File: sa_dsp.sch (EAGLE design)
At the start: 409 parts, among them CN1 uSD, CN2 MINI B USB, CN3 2X5 HEADER, CN4 MINI B USB, CN5 USB A, CN6 MINI B USB, Q1 2N7002, Q2 2N7002, Q3 2N7002, Q4 2N7002, SW1 1825910-7, U1 PGA2311, U10 LME49720, U11 PGA2311, U12 LME49720, U13 LME49720, U14 PCM1754, U15 LME49720, U16 PGA2311, U17 LME49720, U18 LME49720, U19 PCM1754, U2 LM317, U20 LME49720, U21 7 SEG, U22 74HC164A, U23 PCM2707, U24 PCM2707, U25 7 SEG, U26 74HC164A, U27 LM337, U28 LM317, U29 7 SEG, U3 OSD3358-512M-BSM, U30 74HC164A, U31 100MHz, U32 USBLC6-2SC6, U33 FT230X, U34 USBLC6-2SC6, U35 USBLC6-2SC6, U36 USBLC6-2SC6, U37 2 PORT HUB, U38 TPS70925, U39 LM22670, U4 LME49720, U40 MPM3820, U41 MPM3820, U5 LME49720, U6 10CL016YF484C6G, U7 7 SEG, U8 74HC164A, U9 PCM1754

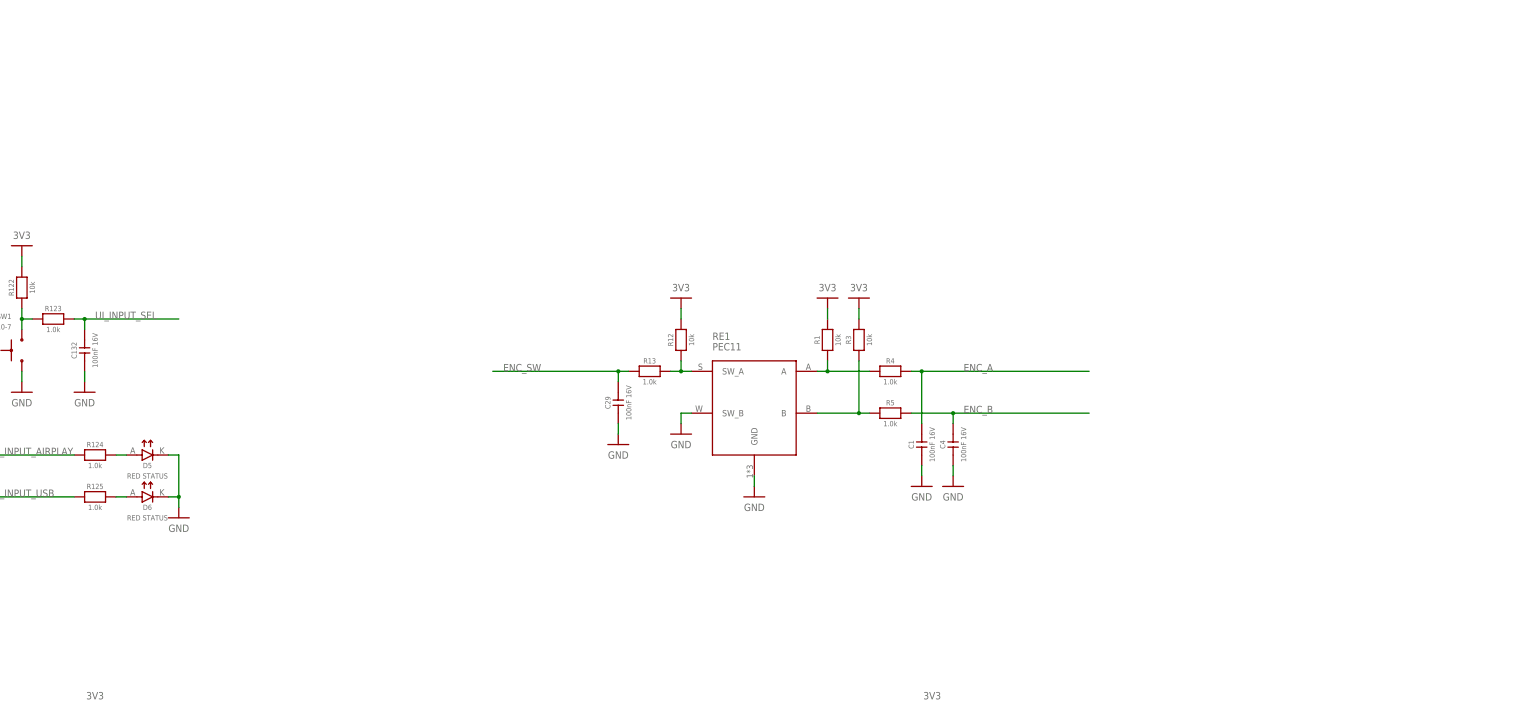
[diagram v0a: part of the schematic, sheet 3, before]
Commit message: Schmit triggers done, FPGA conf done
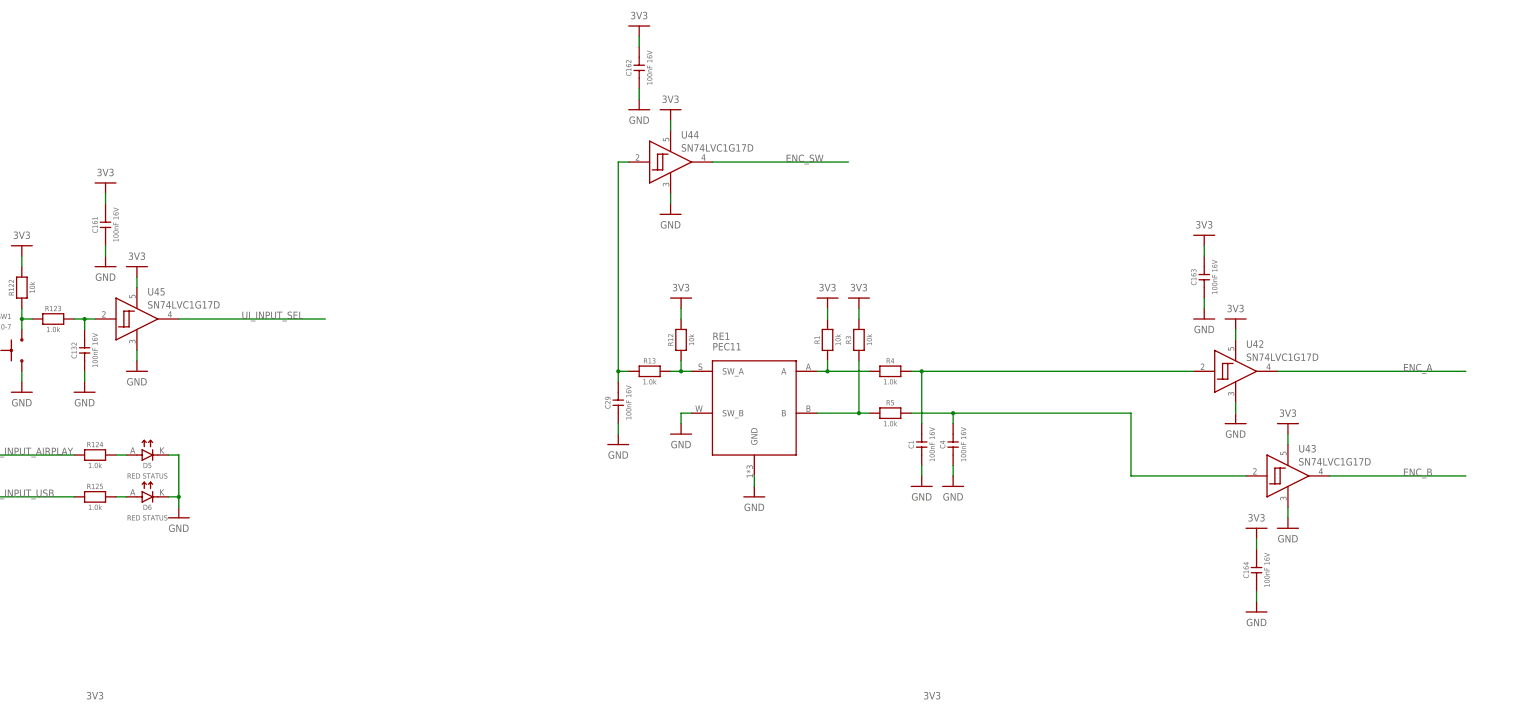
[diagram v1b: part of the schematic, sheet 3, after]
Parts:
- added C161, C162, C163, C164: 100nF 16V, CAPACITORS:CL10B104KO8WPNC
- added U42, U43, U44, U45: SN74LVC1G17D, ICs:SN74LVC1G17DBVR
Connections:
- new net N$238: C4.2, R5.2, U43.A
- new net N$239: C1.2, R4.2, U42.A
- new net N$240: C29.2, R13.1, U44.A
- new net N$241: C132.2, R123.2, U45.A
- net 3V3: now also C161.2, C162.2, C163.2, C164.2, U42.VCC, U43.VCC, U44.VCC, U45.VCC
- net DISP_SPI_!CE: now also U6.B8_IO29
- net DISP_SPI_MOSI: now also U6.B8_IO24
- net DISP_SPI_SCLK: now also U6.B8_IO15
- net ENC_A: now also U42.Q, U6.B8_IO33; no longer C1.2, R4.2
- net ENC_B: now also U43.Q, U6.B8_IO13; no longer C4.2, R5.2
- net ENC_SW: now also U44.Q, U6.B8_IO30; no longer C29.2, R13.1
- net GND: now also C161.1, C162.1, C163.1, C164.1, U42.GND, U43.GND, U44.GND, U45.GND
- net PGA1_SDI: now also U6.B6_IO14; no longer U6.B6_IO16
- net UI_INPUT_AIRPLAY: now also U6.B8_IO25
- net UI_INPUT_SEL: now also U45.Q; no longer C132.2, R123.2
- net UI_INPUT_USB: now also U6.B8_IO16

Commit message: Passes DRC
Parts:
- removed R87: 10k, r_0603:ERJ3EKF1002V
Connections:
- removed net CONF_NCONFIG: R87.1
- net 3V3: no longer R87.2
- net AM_PWR_BTN: now also U6.B2_IO14
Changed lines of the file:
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@@
 <part name="R85" library="r_0603" deviceset="ERJ3EKF1002V" device="" value="10k"/>
 <part name="R86" library="r_0603" deviceset="ERJ3EKF1002V" device="" value="10k"/>
-<part name="R87" library="r_0603" deviceset="ERJ3EKF1002V" device="" value="10k"/>
 <part name="U$163" library="NETS" deviceset="3V3" device=""/>
 <part name="U$164" library="NETS" deviceset="3V3" device=""/>
@@
 <part name="U$166" library="NETS" deviceset="3V3" device=""/>
 <part name="U$167" library="NETS" deviceset="3V3" device=""/>
-<part name="U$168" library="NETS" deviceset="3V3" device=""/>
 <part name="GND78" library="NETS" deviceset="GND" device=""/>
 <part name="GND79" library="NETS" deviceset="GND" device=""/>
@@
 <attribute name="VALUE" x="66.04" y="490.22" size="1.27" layer="96" rot="R90" align="center"/>
 </instance>
-<instance part="R87" gate="G$1" x="71.12" y="490.22" smashed="yes" rot="R90">
-<attribute name="NAME" x="68.58" y="490.22" size="1.27" layer="95" rot="R90" align="center"/>
-<attribute name="VALUE" x="73.66" y="490.22" size="1.27" layer="96" rot="R90" align="center"/>
-</instance>
 <instance part="U$163" gate="G$1" x="33.02" y="472.44" smashed="yes">
 <attribute name="VALUE" x="33.02" y="474.98" size="1.778" layer="96" rot="R180" align="center"/>
@@
 <instance part="U$167" gate="G$1" x="63.5" y="500.38" smashed="yes">
 <attribute name="VALUE" x="63.5" y="502.92" size="1.778" layer="96" rot="R180" align="center"/>
-</instance>
-<instance part="U$168" gate="G$1" x="71.12" y="500.38" smashed="yes">
-<attribute name="VALUE" x="71.12" y="502.92" size="1.778" layer="96" rot="R180" align="center"/>
 </instance>
 <instance part="GND78" gate="G$1" x="43.18" y="426.72" smashed="yes">
@@
 </segment>
 </net>
-<net name="CONF_NCONFIG" class="0">
-<segment>
-<pinref part="R87" gate="G$1" pin="1"/>
-<wire x1="71.12" y1="485.14" x2="71.12" y2="482.6" width="0.1524" layer="91"/>
-<wire x1="71.12" y1="482.6" x2="101.6" y2="482.6" width="0.1524" layer="91"/>
-<label x="73.66" y="482.6" size="1.778" layer="95"/>
-</segment>
-</net>
 <net name="CONF_NSTATUS" class="0">
 <segment>
@@
 <pinref part="U$167" gate="G$1" pin="3V3"/>
 <wire x1="63.5" y1="497.84" x2="63.5" y2="495.3" width="0.1524" layer="91"/>
-</segment>
-<segment>
-<pinref part="R87" gate="G$1" pin="2"/>
-<pinref part="U$168" gate="G$1" pin="3V3"/>
-<wire x1="71.12" y1="497.84" x2="71.12" y2="495.3" width="0.1524" layer="91"/>
 </segment>
 <segment>
@@
 </segment>
 </net>
+<net name="AM_PWR_BTN" class="0">
+<segment>
+<pinref part="U6" gate="G$1" pin="B2_IO14"/>
+<wire x1="312.42" y1="360.68" x2="350.52" y2="360.68" width="0.1524" layer="91"/>
+<label x="314.96" y="360.68" size="1.778" layer="95"/>
+</segment>
+</net>

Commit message: Analogue output connections added
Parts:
- added TP17, TP18, TP19, TP20, TP21, TP22, TP23, TP24, TP25, TP26, TP27, TP28, TP29, TP30, TP31, TP32, TP33, TP34: 2MM_TEST_POINT, MISC:2MM_TEST_POINT
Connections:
- net AGND: now also TP18.P$1, TP21.P$1, TP24.P$1, TP27.P$1, TP30.P$1, TP33.P$1
- net N$100: now also TP19.P$1
- net N$12: now also TP29.P$1
- net N$17: now also TP32.P$1
- net N$28: now also TP34.P$1
- net N$46: now also TP31.P$1
- net N$58: now also TP23.P$1
- net N$60: now also TP26.P$1
- net N$63: now also TP28.P$1
- net N$73: now also TP25.P$1
- net N$85: now also TP17.P$1
- net N$87: now also TP20.P$1
- net N$90: now also TP22.P$1
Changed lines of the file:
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@@
 <part name="GND181" library="NETS" deviceset="GND" device=""/>
 <part name="U$223" library="NETS" deviceset="3V3" device=""/>
+<part name="TP17" library="MISC" deviceset="2MM_TEST_POINT" device=""/>
+<part name="TP18" library="MISC" deviceset="2MM_TEST_POINT" device=""/>
+<part name="TP19" library="MISC" deviceset="2MM_TEST_POINT" device=""/>
+<part name="TP20" library="MISC" deviceset="2MM_TEST_POINT" device=""/>
+<part name="TP21" library="MISC" deviceset="2MM_TEST_POINT" device=""/>
+<part name="TP22" library="MISC" deviceset="2MM_TEST_POINT" device=""/>
+<part name="TP23" library="MISC" deviceset="2MM_TEST_POINT" device=""/>
+<part name="TP24" library="MISC" deviceset="2MM_TEST_POINT" device=""/>
+<part name="TP25" library="MISC" deviceset="2MM_TEST_POINT" device=""/>
+<part name="TP26" library="MISC" deviceset="2MM_TEST_POINT" device=""/>
+<part name="TP27" library="MISC" deviceset="2MM_TEST_POINT" device=""/>
+<part name="TP28" library="MISC" deviceset="2MM_TEST_POINT" device=""/>
+<part name="TP29" library="MISC" deviceset="2MM_TEST_POINT" device=""/>
+<part name="TP30" library="MISC" deviceset="2MM_TEST_POINT" device=""/>
+<part name="TP31" library="MISC" deviceset="2MM_TEST_POINT" device=""/>
+<part name="TP32" library="MISC" deviceset="2MM_TEST_POINT" device=""/>
+<part name="TP33" library="MISC" deviceset="2MM_TEST_POINT" device=""/>
+<part name="TP34" library="MISC" deviceset="2MM_TEST_POINT" device=""/>
+<part name="U$168" library="NETS" deviceset="AGND" device=""/>
 </parts>
 <sheets>
@@
 <attribute name="VALUE" x="43.18" y="657.86" size="1.27" layer="96" rot="MR0" align="center-left"/>
 </instance>
+<instance part="TP17" gate="G$1" x="457.2" y="662.94" smashed="yes" rot="R270">
+<attribute name="NAME" x="459.74" y="662.94" size="1.27" layer="97" rot="R270" align="center"/>
+</instance>
+<instance part="TP18" gate="G$1" x="474.98" y="647.7" smashed="yes" rot="R270">
+<attribute name="NAME" x="477.52" y="647.7" size="1.27" layer="97" rot="R270" align="center"/>
+</instance>
+<instance part="TP19" gate="G$1" x="457.2" y="632.46" smashed="yes" rot="R270">
+<attribute name="NAME" x="459.74" y="632.46" size="1.27" layer="97" rot="R270" align="center"/>
+</instance>
+<instance part="TP20" gate="G$1" x="457.2" y="591.82" smashed="yes" rot="R270">
+<attribute name="NAME" x="459.74" y="591.82" size="1.27" layer="97" rot="R270" align="center"/>
+</instance>
+<instance part="TP21" gate="G$1" x="474.98" y="579.12" smashed="yes" rot="R270">
+<attribute name="NAME" x="477.52" y="579.12" size="1.27" layer="97" rot="R270" align="center"/>
+</instance>
+<instance part="TP22" gate="G$1" x="457.2" y="561.34" smashed="yes" rot="R270">
+<attribute name="NAME" x="459.74" y="561.34" size="1.27" layer="97" rot="R270" align="center"/>
+</instance>
+<instance part="TP23" gate="G$1" x="457.2" y="408.94" smashed="yes" rot="R270">
+<attribute name="NAME" x="459.74" y="408.94" size="1.27" layer="97" rot="R270" align="center"/>
+</instance>
+<instance part="TP24" gate="G$1" x="474.98" y="396.24" smashed="yes" rot="R270">
+<attribute name="NAME" x="477.52" y="396.24" size="1.27" layer="97" rot="R270" align="center"/>
+</instance>
+<instance part="TP25" gate="G$1" x="457.2" y="378.46" smashed="yes" rot="R270">
+<attribute name="NAME" x="459.74" y="378.46" size="1.27" layer="97" rot="R270" align="center"/>
+</instance>
+<instance part="TP26" gate="G$1" x="457.2" y="337.82" smashed="yes" rot="R270">
+<attribute name="NAME" x="459.74" y="337.82" size="1.27" layer="97" rot="R270" align="center"/>
+</instance>
+<instance part="TP27" gate="G$1" x="474.98" y="327.66" smashed="yes" rot="R270">
+<attribute name="NAME" x="477.52" y="327.66" size="1.27" layer="97" rot="R270" align="center"/>
+</instance>
+<instance part="TP28" gate="G$1" x="457.2" y="307.34" smashed="yes" rot="R270">
+<attribute name="NAME" x="459.74" y="307.34" size="1.27" layer="97" rot="R270" align="center"/>
+</instance>
+<instance part="TP29" gate="G$1" x="457.2" y="154.94" smashed="yes" rot="R270">
+<attribute name="NAME" x="459.74" y="154.94" size="1.27" layer="97" rot="R270" align="center"/>
+</instance>
+<instance part="TP30" gate="G$1" x="474.98" y="142.24" smashed="yes" rot="R270">
+<attribute name="NAME" x="477.52" y="142.24" size="1.27" layer="97" rot="R270" align="center"/>
+</instance>
+<instance part="TP31" gate="G$1" x="457.2" y="124.46" smashed="yes" rot="R270">
+<attribute name="NAME" x="459.74" y="124.46" size="1.27" layer="97" rot="R270" align="center"/>
+</instance>
+<instance part="TP32" gate="G$1" x="457.2" y="83.82" smashed="yes" rot="R270">
+<attribute name="NAME" x="459.74" y="83.82" size="1.27" layer="97" rot="R270" align="center"/>
+</instance>
+<instance part="TP33" gate="G$1" x="474.98" y="71.12" smashed="yes" rot="R270">
+<attribute name="NAME" x="477.52" y="71.12" size="1.27" layer="97" rot="R270" align="center"/>
+</instance>
+<instance part="TP34" gate="G$1" x="457.2" y="53.34" smashed="yes" rot="R270">
+<attribute name="NAME" x="459.74" y="53.34" size="1.27" layer="97" rot="R270" align="center"/>
+</instance>
+<instance part="U$168" gate="G$1" x="467.36" y="66.04" smashed="yes">
+<attribute name="VALUE" x="467.36" y="63.5" size="1.778" layer="96" align="center"/>
+</instance>
 </instances>
 <busses>
@@
 <junction x="401.32" y="154.94"/>
 <wire x1="401.32" y1="154.94" x2="452.12" y2="154.94" width="0.1524" layer="91"/>
+<pinref part="TP29" gate="G$1" pin="P$1"/>
 </segment>
 </net>
@@
 <junction x="393.7" y="83.82"/>
 <wire x1="393.7" y1="83.82" x2="452.12" y2="83.82" width="0.1524" layer="91"/>
+<pinref part="TP32" gate="G$1" pin="P$1"/>
 </segment>
 </net>
@@
 <wire x1="449.58" y1="53.34" x2="452.12" y2="53.34" width="0.1524" layer="91"/>
 <pinref part="R21" gate="G$1" pin="2"/>
+<pinref part="TP34" gate="G$1" pin="P$1"/>
 </segment>
 </net>
@@
 <pinref part="C82" gate="G$1" pin="2"/>
 </segment>
+<segment>
+<pinref part="TP18" gate="G$1" pin="P$1"/>
+<wire x1="469.9" y1="647.7" x2="467.36" y2="647.7" width="0.1524" layer="91"/>
+<wire x1="467.36" y1="647.7" x2="467.36" y2="579.12" width="0.1524" layer="91"/>
+<pinref part="TP33" gate="G$1" pin="P$1"/>
+<wire x1="467.36" y1="579.12" x2="467.36" y2="546.1" width="0.1524" layer="91"/>
+<wire x1="467.36" y1="546.1" x2="467.36" y2="396.24" width="0.1524" layer="91"/>
+<wire x1="467.36" y1="396.24" x2="467.36" y2="327.66" width="0.1524" layer="91"/>
+<wire x1="467.36" y1="327.66" x2="467.36" y2="142.24" width="0.1524" layer="91"/>
+<wire x1="467.36" y1="142.24" x2="467.36" y2="71.12" width="0.1524" layer="91"/>
+<wire x1="467.36" y1="71.12" x2="469.9" y2="71.12" width="0.1524" layer="91"/>
+<pinref part="TP30" gate="G$1" pin="P$1"/>
+<wire x1="467.36" y1="142.24" x2="469.9" y2="142.24" width="0.1524" layer="91"/>
+<junction x="467.36" y="142.24"/>
+<pinref part="TP27" gate="G$1" pin="P$1"/>
+<wire x1="467.36" y1="327.66" x2="469.9" y2="327.66" width="0.1524" layer="91"/>
+<junction x="467.36" y="327.66"/>
+<pinref part="TP24" gate="G$1" pin="P$1"/>
+<wire x1="469.9" y1="396.24" x2="467.36" y2="396.24" width="0.1524" layer="91"/>
+<junction x="467.36" y="396.24"/>
+<pinref part="TP21" gate="G$1" pin="P$1"/>
+<wire x1="469.9" y1="579.12" x2="467.36" y2="579.12" width="0.1524" layer="91"/>
+<junction x="467.36" y="579.12"/>
+<pinref part="U$168" gate="G$1" pin="AGND"/>
+<wire x1="467.36" y1="68.58" x2="467.36" y2="71.12" width="0.1524" layer="91"/>
+<junction x="467.36" y="71.12"/>
+</segment>
 </net>
 <net name="N$46" class="0">
@@
 <wire x1="449.58" y1="124.46" x2="452.12" y2="124.46" width="0.1524" layer="91"/>
 <pinref part="R17" gate="G$1" pin="2"/>
+<pinref part="TP31" gate="G$1" pin="P$1"/>
 </segment>
 </net>
@@
 <junction x="401.32" y="408.94"/>
 <wire x1="401.32" y1="408.94" x2="452.12" y2="408.94" width="0.1524" layer="91"/>
+<pinref part="TP23" gate="G$1" pin="P$1"/>
 </segment>
 </net>
@@
 <junction x="393.7" y="337.82"/>
 <wire x1="393.7" y1="337.82" x2="452.12" y2="337.82" width="0.1524" layer="91"/>
+<pinref part="TP26" gate="G$1" pin="P$1"/>
 </segment>
 </net>
@@
 <wire x1="449.58" y1="307.34" x2="452.12" y2="307.34" width="0.1524" layer="91"/>
 <pinref part="R32" gate="G$1" pin="2"/>
+<pinref part="TP28" gate="G$1" pin="P$1"/>
 </segment>
 </net>
@@
 <wire x1="449.58" y1="378.46" x2="452.12" y2="378.46" width="0.1524" layer="91"/>
 <pinref part="R30" gate="G$1" pin="2"/>
+<pinref part="TP25" gate="G$1" pin="P$1"/>
 </segment>
 </net>
@@
 <junction x="401.32" y="662.94"/>
 <wire x1="401.32" y1="662.94" x2="452.12" y2="662.94" width="0.1524" layer="91"/>
+<pinref part="TP17" gate="G$1" pin="P$1"/>
 </segment>
 </net>
@@
 <junction x="393.7" y="591.82"/>
 <wire x1="393.7" y1="591.82" x2="452.12" y2="591.82" width="0.1524" layer="91"/>
+<pinref part="TP20" gate="G$1" pin="P$1"/>
 </segment>
 </net>
@@
 <wire x1="449.58" y1="561.34" x2="452.12" y2="561.34" width="0.1524" layer="91"/>
 <pinref part="R43" gate="G$1" pin="2"/>
+<pinref part="TP22" gate="G$1" pin="P$1"/>
 </segment>
 </net>
@@
 <wire x1="449.58" y1="632.46" x2="452.12" y2="632.46" width="0.1524" layer="91"/>
 <pinref part="R41" gate="G$1" pin="2"/>
+<pinref part="TP19" gate="G$1" pin="P$1"/>
 </segment>
 </net>

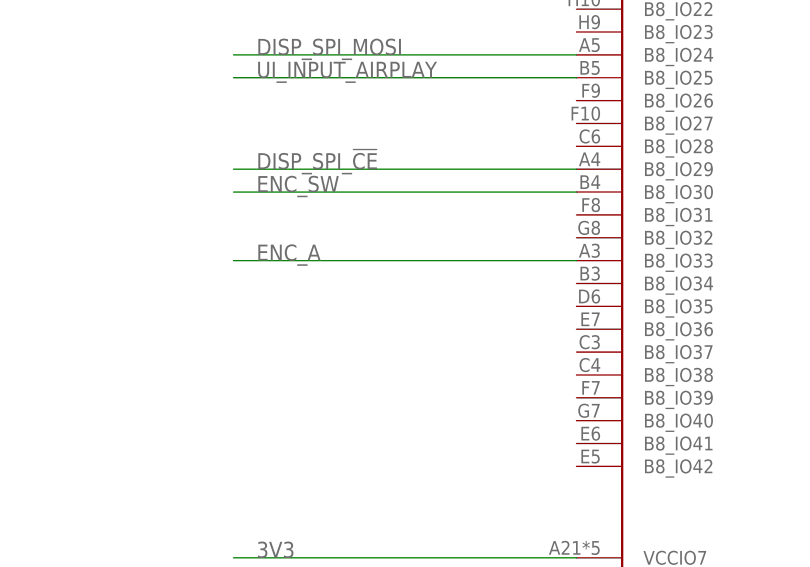
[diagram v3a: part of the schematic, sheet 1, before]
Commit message: Connect mode button
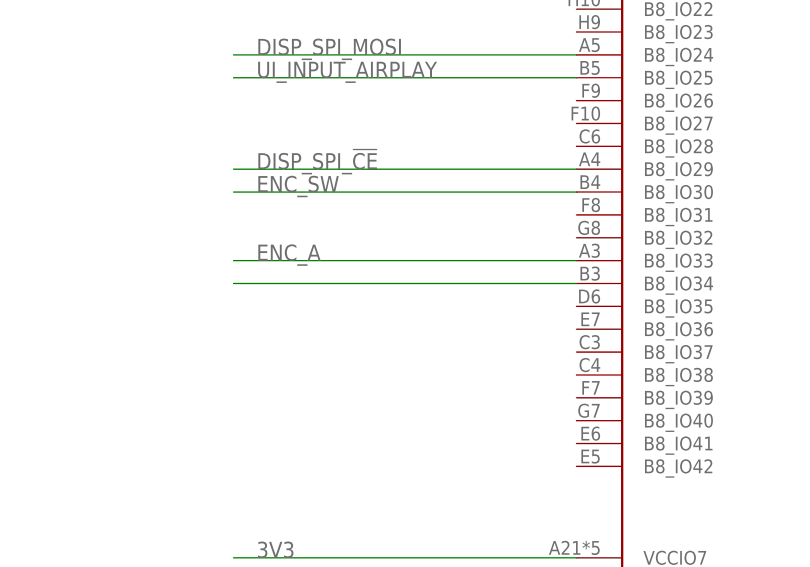
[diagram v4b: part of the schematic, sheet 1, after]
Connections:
- net UI_INPUT_SEL: now also U6.B8_IO34
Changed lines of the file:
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@@
+</segment>
+</net>
+<net name="UI_INPUT_SEL" class="0">
+<segment>
+<pinref part="U6" gate="G$1" pin="B8_IO34"/>
+<wire x1="226.06" y1="439.42" x2="187.96" y2="439.42" width="0.1524" layer="91"/>
 </segment>
 </net>
